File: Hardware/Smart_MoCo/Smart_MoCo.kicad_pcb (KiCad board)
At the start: 4 copper layers, 26.9 x 39.9 mm, 32 parts, among them J1 Conn_01x02, J2 Conn_01x04, J3 Conn_01x02, J4 Conn_01x02, J5 Conn_01x04, J6 1722861102, J7 1722861102, U1 STM32F042F6Px, U2 VNH5019A-E, U3 SN65HVD232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

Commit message: Added bulk capacitors and kicad github action
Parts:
- added C4: 100nF, Capacitor_SMD:C_0402_1005Metric_Pad0.74x0.62mm_HandSolder, F.Cu at (159.5, 91.3)
- added C5: 100nF, Capacitor_SMD:C_0402_1005Metric_Pad0.74x0.62mm_HandSolder, F.Cu at (158.5, 91.3)
- added C6: 4.7uF, Capacitor_SMD:C_0402_1005Metric_Pad0.74x0.62mm_HandSolder, F.Cu at (158.5, 89.0)
- added C7: 10nF, Capacitor_SMD:C_0402_1005Metric_Pad0.74x0.62mm_HandSolder, F.Cu at (157.4, 91.3)
- added C8: 1uF, Capacitor_SMD:C_0402_1005Metric_Pad0.74x0.62mm_HandSolder, F.Cu at (156.3, 91.3)
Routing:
- net +3V3: track 16.5 -> 22.3 mm, vias 9 -> 11
- net GND: track 4.58 -> 10.1 mm, vias 17 -> 20
- net SWCLK: track 5.32 -> 6.51 mm
- net CS: track 6.36 -> 6.95 mm
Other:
- board text added: "3V3 C D G"
- board text added: "SWD"
- board text removed: "SWD 3V3 C D G"

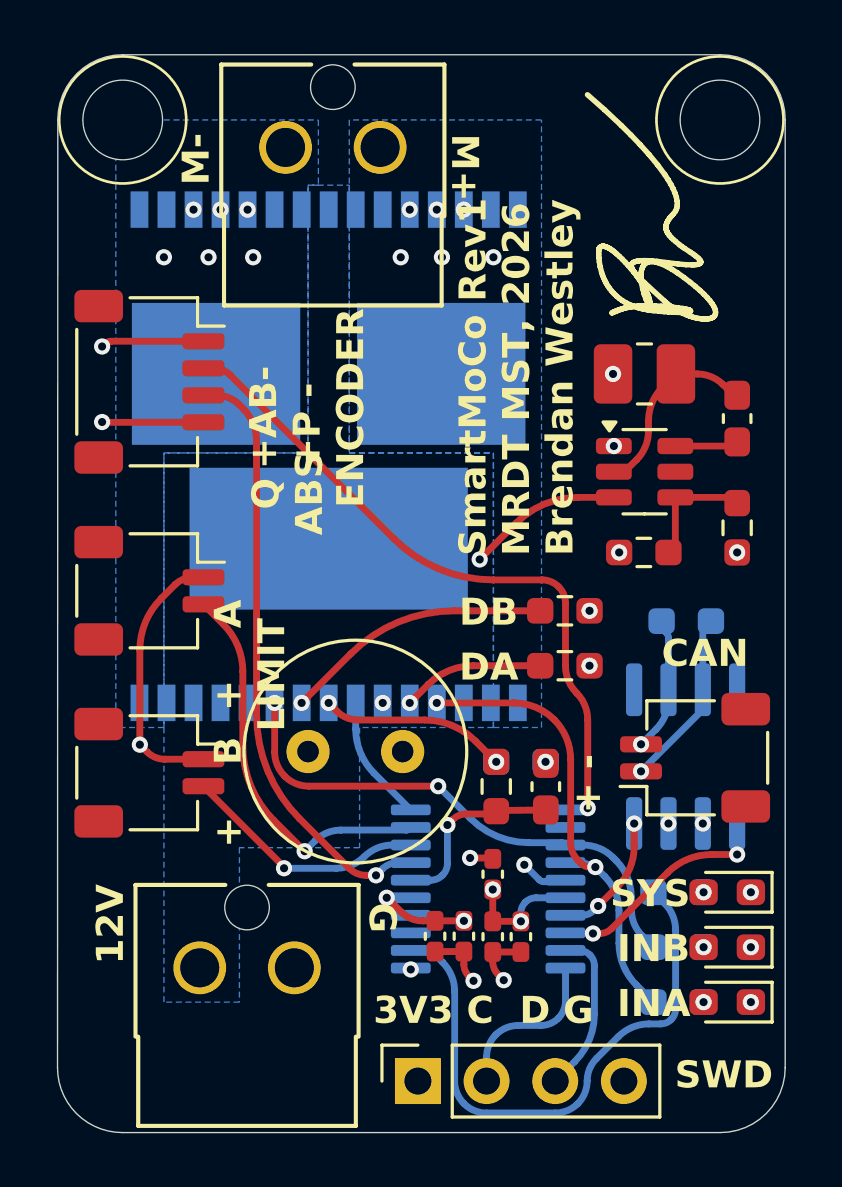
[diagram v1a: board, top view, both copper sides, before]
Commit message: Via stitch 12V and OUT planes
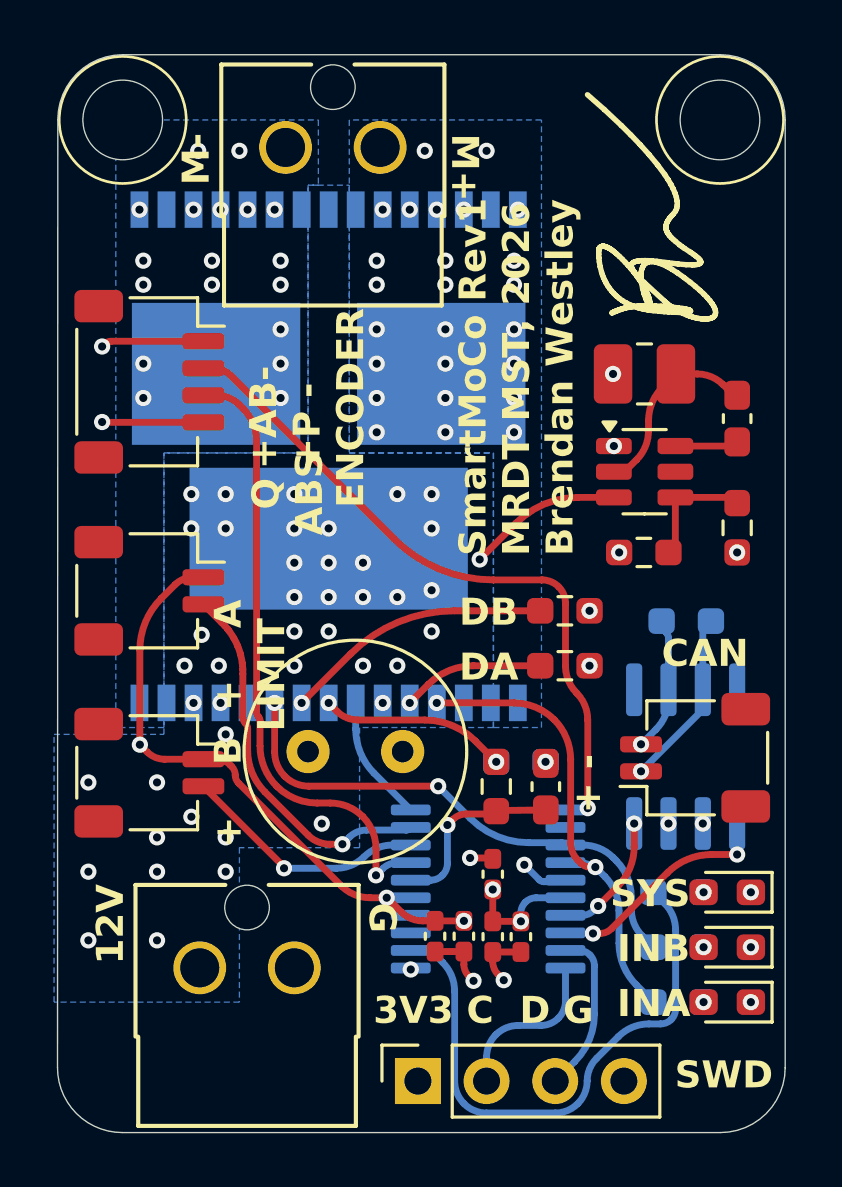
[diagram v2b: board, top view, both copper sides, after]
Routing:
- net +3V3: track 22.3 -> 31.3 mm
- net ENC_B: track 22.4 -> 23.1 mm
- net LIM_B: track 14.6 -> 14.0 mm
- net +12V: vias 1 -> 42
- net /OUTB: vias 3 -> 15
- net /OUTA: vias 3 -> 22

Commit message: Update via stitching
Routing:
- net +12V: vias 42 -> 46

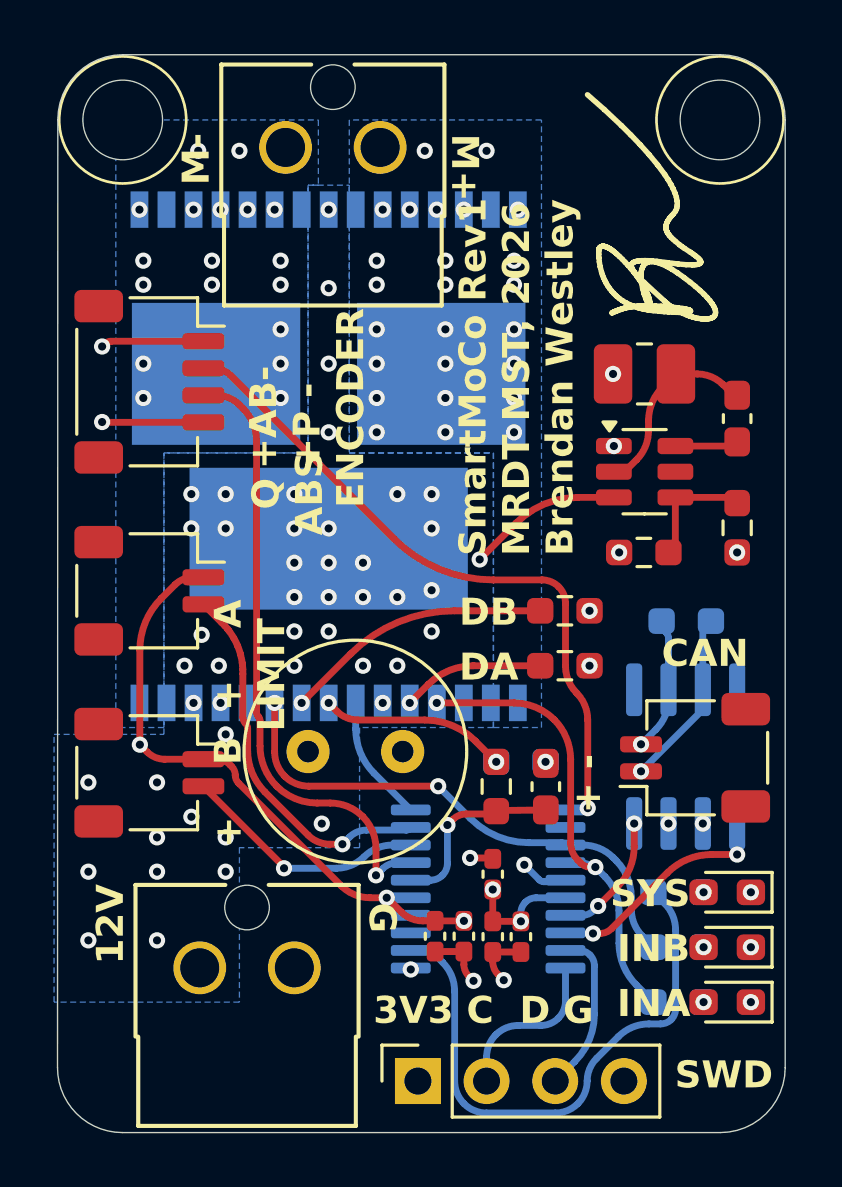
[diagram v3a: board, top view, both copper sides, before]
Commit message: Fix vias on edges of pads
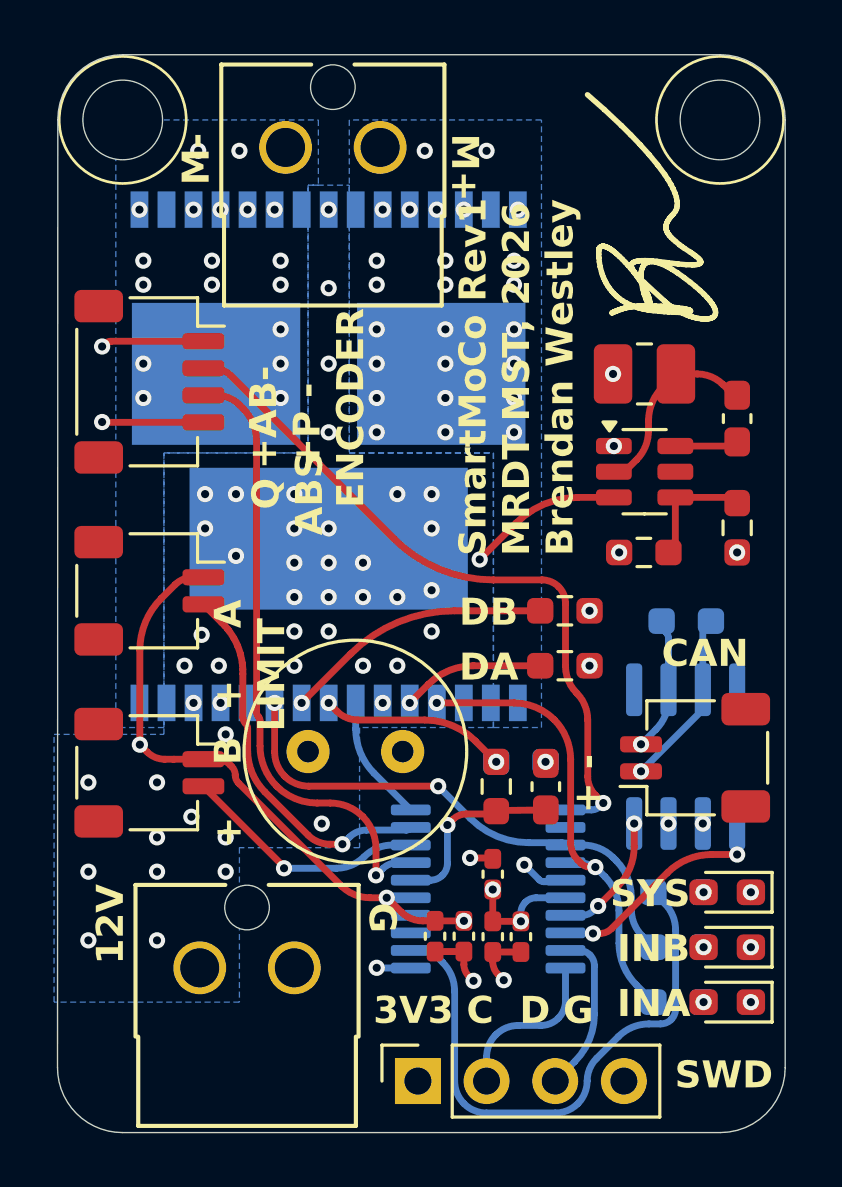
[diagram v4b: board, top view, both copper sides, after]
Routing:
- net GND: track 10.1 -> 11.3 mm
- net ENC_A/PWM: track 25.5 -> 26.1 mm
